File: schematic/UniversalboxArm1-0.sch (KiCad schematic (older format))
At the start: 170 parts, among them J1 USB_B_Micro, J110 Conn_01x03_Male, J120 Conn_02x04_Counter_Clockwise, J121 Conn_01x02_Male, J20 AVR-ISP-6, J50 Conn_01x14_Female, J60 Conn_01x06_Female, J61 Conn_02x08_Odd_Even, J62 Conn_02x04_Odd_Even, J90 Conn_02x03_Odd_Even, J91 Conn_02x04_Odd_Even, K90 IM01, K91 IM01, K92 IM01, K93 IM01, Q120 IRLML6402, Q20 BCX56-16, Q21 BSS138, Q22 BSS138, Q23 IRLML6402, Q24 IRLML6402, Q25 BSS138, Q50 IRLML6402, Q51 IRLML6402, Q60 BSS138, Q61 BSS138, Q62 BSS138, Q90 BSS138, Q91 BSS138, Q92 BSS138, Q93 BSS138, SW60 SW_SPST, SW61 SW_SPST, SW62 SW_SPST, SW63 SW_SPST, U1 USBLC6-2SC6, U110 MAX3221, U130 TSOP312xx, U2 LP38693MP-3.3, U20 ATtiny861A-SU, U21 REF3020, U22 MCP6542, U50 AT45DB641-S, U60 STM32L452RETx, U61 MCP65R41T-1202E, Y60 16MHz, Y61 32768Hz

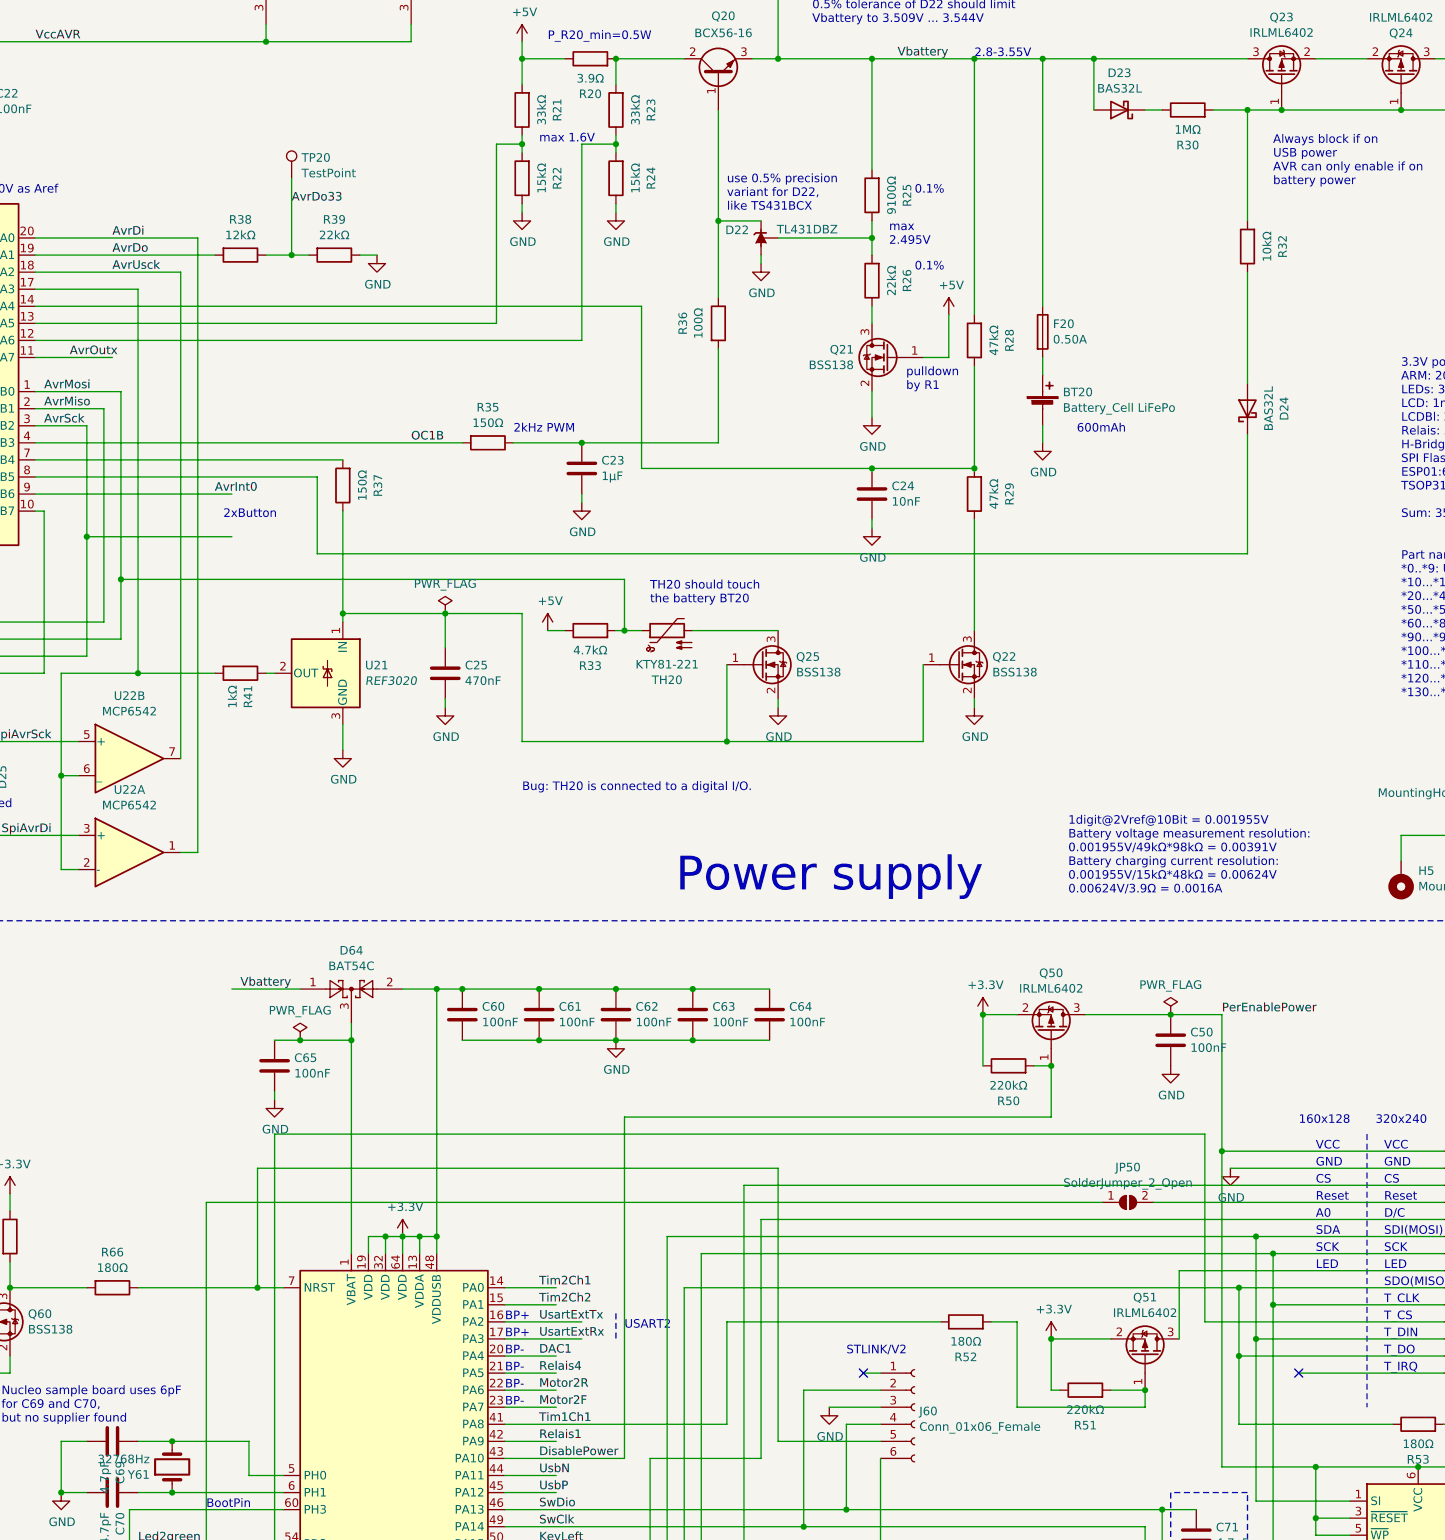
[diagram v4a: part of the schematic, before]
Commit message: Update schematic to version 1 revision 0.5 Reflecting issues found while getting pcb to work
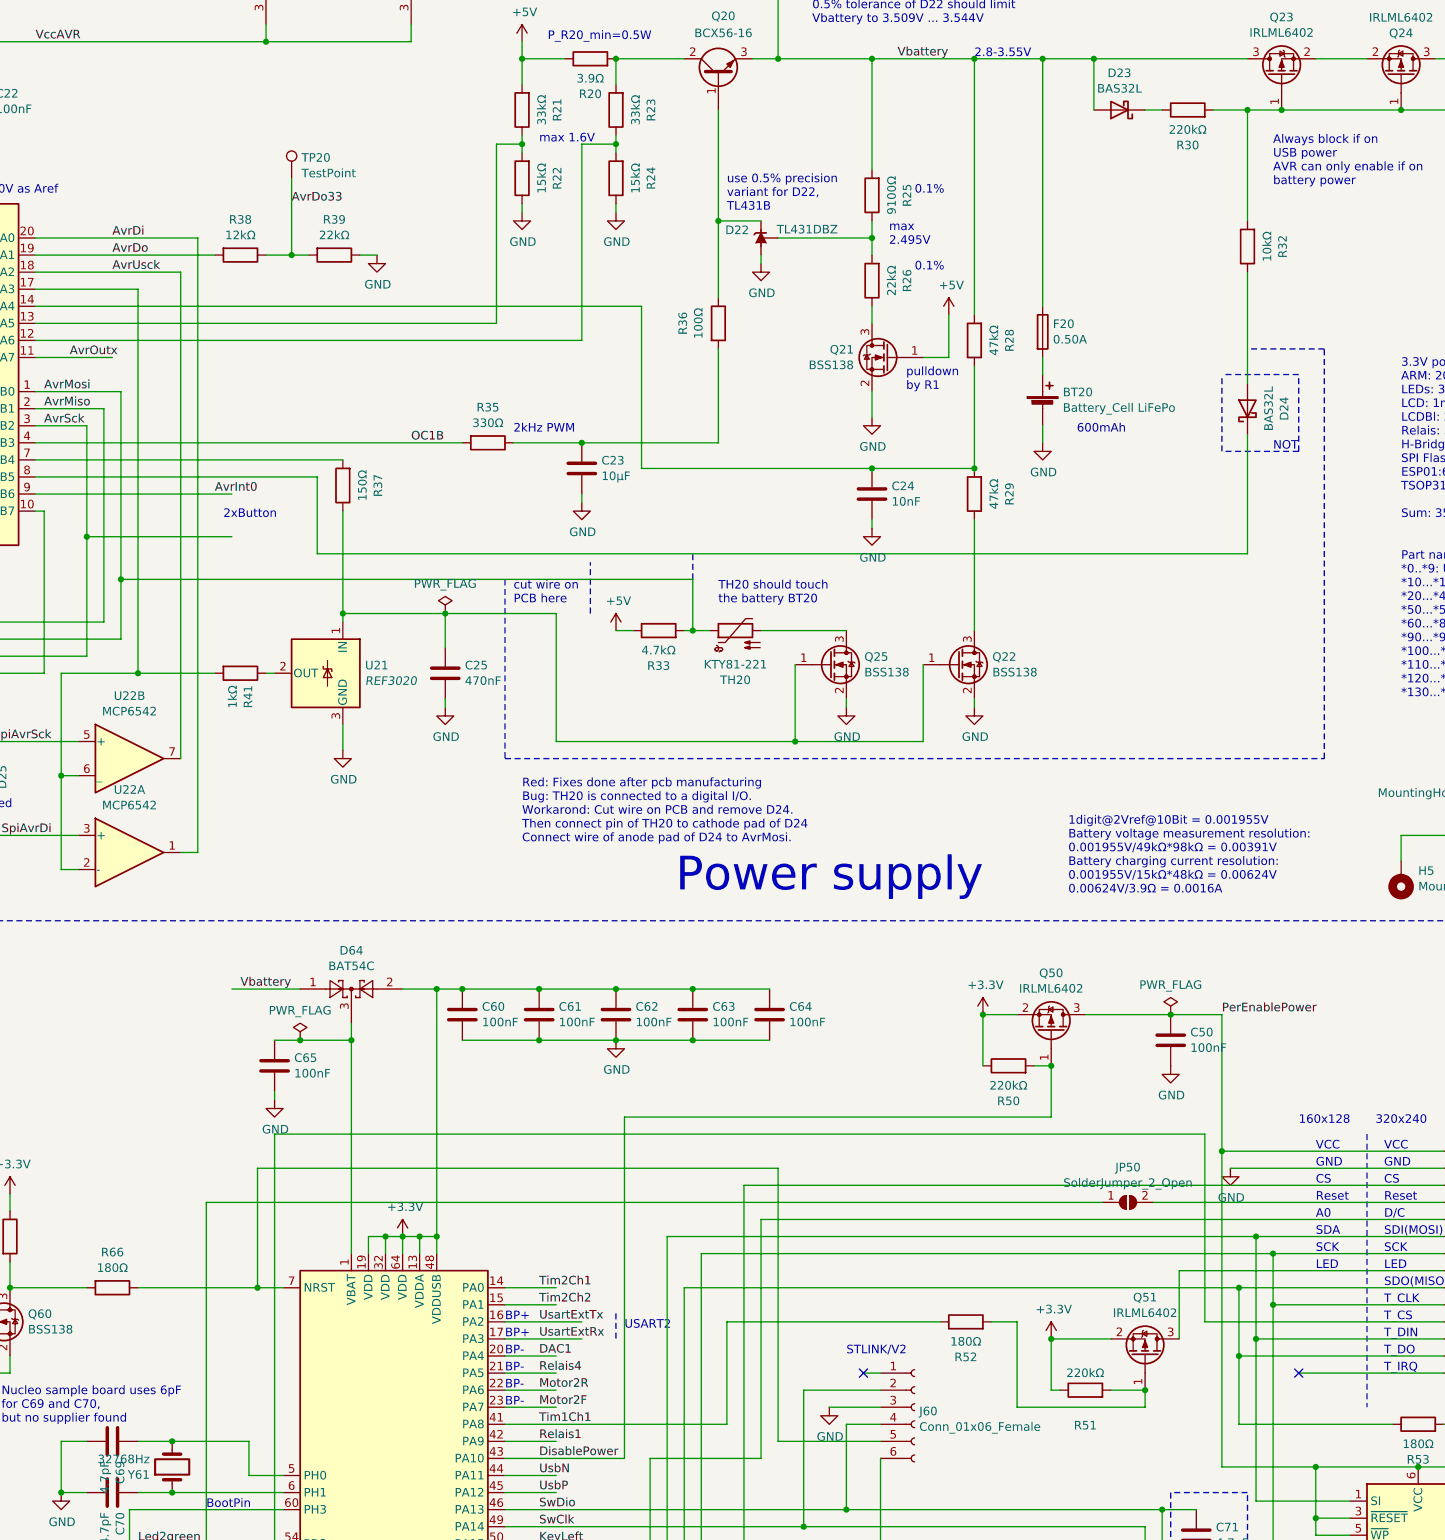
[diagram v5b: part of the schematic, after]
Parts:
- C23: value 1µF -> 10µF
- R30: value 1MΩ -> 220kΩ
- R35: value 150Ω -> 330Ω
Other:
- note added: "NOT"
- note added: "Red: Fixes done after pcb manufacturing\nBug: TH20 is connected to a digital I/O.\nWorkarond: Cut wire on PCB and remove D24.\nThen connect pin of TH20 to cathode pad of D24\nConnect wire of anode pad of D24 to AvrMosi."
- note added: "cut wire on\nPCB here"
- note added: "use 0.5% precision\nvariant for D22,\nTL431B\n"
- note removed: "Bug: TH20 is connected to a digital I/O."
- note removed: "use 0.5% precision\nvariant for D22,\nlike TS431BCX\n"
- moved on the sheet: Q25, R33, TH20
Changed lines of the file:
@@
 Sheet 1 1
 Title ""
-Date "2021-12-04"
-Rev "0.4"
+Date "2021-12-18"
+Rev "0.5"
 Comp ""
 Comment1 ""
@@
 P 4950 5450
 F 0 "R35" V 4743 5450 50  0000 C CNN
-F 1 "150Ω" V 4834 5450 50  0000 C CNN
+F 1 "330Ω" V 4834 5450 50  0000 C CNN
 F 2 "Resistor_SMD:R_0805_2012Metric_Pad1.15x1.40mm_HandSolder" V 4880 5450 50  0001 C CNN
 F 3 "~" H 4950 5450 50  0001 C CNN
@@
 P 5500 5600
 F 0 "C23" H 5615 5646 50  0000 L CNN
-F 1 "1µF" H 5615 5555 50  0000 L CNN
+F 1 "10µF" H 5615 5555 50  0000 L CNN
 F 2 "Capacitor_SMD:C_0805_2012Metric_Pad1.15x1.40mm_HandSolder" H 5538 5450 50  0001 C CNN
 F 3 "~" H 5500 5600 50  0001 C CNN
@@
 P 9050 3500
 F 0 "R30" V 8843 3500 50  0000 C CNN
-F 1 "1MΩ" V 8934 3500 50  0000 C CNN
+F 1 "220kΩ" V 8934 3500 50  0000 C CNN
 F 2 "Resistor_SMD:R_0805_2012Metric_Pad1.15x1.40mm_HandSolder" V 8980 3500 50  0001 C CNN
 F 3 "~" H 9050 3500 50  0001 C CNN
@@
 	6300 4150 6550 4150
 Text Notes 6350 4100 0    50   ~ 0
-use 0.5% precision\nvariant for D22,\nlike TS431BCX\n
+use 0.5% precision\nvariant for D22,\nTL431B\n
 $Comp
 L power:GND #PWR0121
@@
 L power:GND #PWR0124
 U 1 1 60A081EA
-P 6650 7000
-F 0 "#PWR0124" H 6650 6750 50  0001 C CNN
-F 1 "GND" H 6655 6827 50  0000 C CNN
-F 2 "" H 6650 7000 50  0001 C CNN
-F 3 "" H 6650 7000 50  0001 C CNN
-	1    6650 7000
+P 7050 7000
+F 0 "#PWR0124" H 7050 6750 50  0001 C CNN
+F 1 "GND" H 7055 6827 50  0000 C CNN
+F 2 "" H 7050 7000 50  0001 C CNN
+F 3 "" H 7050 7000 50  0001 C CNN
+	1    7050 7000
 	1    0    0    -1
 $EndComp
@@
 	6650 4250 7200 4250
 Wire Wire Line
-	6650 7000 6650 6950
+	7050 7000 7050 6950
 $Comp
 L Device:C C24
@@
 L Device:R R33
 U 1 1 609D221A
-P 5550 6550
-F 0 "R33" V 5343 6550 50  0000 C CNN
-F 1 "4.7kΩ" V 5434 6550 50  0000 C CNN
-F 2 "Resistor_SMD:R_0805_2012Metric_Pad1.15x1.40mm_HandSolder" V 5480 6550 50  0001 C CNN
-F 3 "~" H 5550 6550 50  0001 C CNN
-	1    5550 6550
+P 5950 6550
+F 0 "R33" V 5743 6550 50  0000 C CNN
+F 1 "4.7kΩ" V 5834 6550 50  0000 C CNN
+F 2 "Resistor_SMD:R_0805_2012Metric_Pad1.15x1.40mm_HandSolder" V 5880 6550 50  0001 C CNN
+F 3 "~" H 5950 6550 50  0001 C CNN
+	1    5950 6550
 	0    -1   -1   0
 $EndComp
-Text Notes 5900 6400 0    50   ~ 0
+Text Notes 6300 6400 0    50   ~ 0
 TH20 should touch\nthe battery BT20
 Text Label 3350 5750 0    50   ~ 0
@@
 	9400 6100 9400 5400
 Wire Wire Line
-	5850 6550 5750 6550
+	6250 6550 6150 6550
 $Comp
 L power:+5V #PWR0140
 U 1 1 60B19109
-P 5300 6550
-F 0 "#PWR0140" H 5300 6400 50  0001 C CNN
-F 1 "+5V" H 5315 6723 50  0000 C CNN
-F 2 "" H 5300 6550 50  0001 C CNN
-F 3 "" H 5300 6550 50  0001 C CNN
-	1    5300 6550
+P 5700 6550
+F 0 "#PWR0140" H 5700 6400 50  0001 C CNN
+F 1 "+5V" H 5715 6723 50  0000 C CNN
+F 2 "" H 5700 6550 50  0001 C CNN
+F 3 "" H 5700 6550 50  0001 C CNN
+	1    5700 6550
 	1    0    0    -1
 $EndComp
 Wire Wire Line
-	5400 6550 5300 6550
-Connection ~ 5750 6550
+	5800 6550 5700 6550
+Connection ~ 6150 6550
 Wire Wire Line
-	5750 6550 5700 6550
+	6150 6550 6100 6550
 Wire Wire Line
-	5150 6450 5150 7200
+	5350 6450 5350 7200
 Wire Wire Line
-	5150 7200 6350 7200
+	5350 7200 6750 7200
 Wire Wire Line
-	4700 6450 5150 6450
+	4700 6450 5350 6450
 Connection ~ 4700 6450
 $Comp
 L Sensor_Temperature:KTY81 TH20
 U 1 1 60B8406D
-P 6000 6550
-F 0 "TH20" V 5710 6550 50  0000 C CNN
-F 1 "KTY81-221" V 5801 6550 50  0000 C CNN
-F 2 "Package_TO_SOT_THT:TO-92-2" V 6200 6550 50  0001 C CNN
-F 3 "http://www.nxp.com/documents/data_sheet/KTY81_SER.pdf" H 6000 6500 50  0001 C CNN
-	1    6000 6550
+P 6400 6550
+F 0 "TH20" V 6110 6550 50  0000 C CNN
+F 1 "KTY81-221" V 6201 6550 50  0000 C CNN
+F 2 "Package_TO_SOT_THT:TO-92-2" V 6600 6550 50  0001 C CNN
+F 3 "http://www.nxp.com/documents/data_sheet/KTY81_SER.pdf" H 6400 6500 50  0001 C CNN
+	1    6400 6550
 	0    -1   -1   0
 $EndComp
@@
 AvrDo33
 Wire Wire Line
-	2800 6250 5750 6250
+	2800 6250 6150 6250
 Connection ~ 2800 6250
 Wire Wire Line
 	2800 6250 2800 6600
 Wire Wire Line
-	5750 6250 5750 6550
+	6150 6250 6150 6550
 Wire Wire Line
 	2300 4950 2750 4950
@@
 L Transistor_FET:BSS138 Q25
 U 1 1 60B55064
-P 6550 6750
-F 0 "Q25" H 6755 6796 50  0000 L CNN
-F 1 "BSS138" H 6755 6705 50  0000 L CNN
-F 2 "Package_TO_SOT_SMD:SOT-23" H 6750 6675 50  0001 L CIN
-F 3 "https://www.fairchildsemi.com/datasheets/BS/BSS138.pdf" H 6550 6750 50  0001 L CNN
-	1    6550 6750
+P 6950 6750
+F 0 "Q25" H 7155 6796 50  0000 L CNN
+F 1 "BSS138" H 7155 6705 50  0000 L CNN
+F 2 "Package_TO_SOT_SMD:SOT-23" H 7150 6675 50  0001 L CIN
+F 3 "https://www.fairchildsemi.com/datasheets/BS/BSS138.pdf" H 6950 6750 50  0001 L CNN
+	1    6950 6750
 	1    0    0    -1
 $EndComp
@@
 $EndComp
 Wire Wire Line
-	6150 6550 6650 6550
+	6550 6550 7050 6550
 Wire Wire Line
-	6350 6750 6350 7200
-Connection ~ 6350 7200
+	6750 6750 6750 7200
+Connection ~ 6750 7200
 $Comp
 L power:GND #PWR0144
@@
 P 8450 11000
 F 0 "R51" V 8243 11000 50  0000 C CNN
-F 1 "220kΩ" V 8334 11000 50  0000 C CNN
+F 1 "220kΩ" V 8550 11000 50  0000 C CNN
 F 2 "Resistor_SMD:R_0805_2012Metric_Pad1.15x1.40mm_HandSolder" V 8380 11000 50  0001 C CNN
 F 3 "~" H 8450 11000 50  0001 C CNN
@@
 Text Notes 10300 6950 0    50   ~ 0
 Part naming conventions:\n*0..*9: USB Vin\n*10...*19: reserved\n*20...*49: Battery Vin\n*50...*59: LCD and flash\n*60...*89: ARM CPU + basics\n*90...*99: Relais\n*100...*109: Reserved\n*110...*119: RS232\n*120...*129: ESP-01\n*130...*139: TSOP31236
-Text Notes 5150 7500 0    50   ~ 0
-Bug: TH20 is connected to a digital I/O.
+Text Notes 5150 7800 0    50   ~ 0
+Red: Fixes done after pcb manufacturing\nBug: TH20 is connected to a digital I/O.\nWorkarond: Cut wire on PCB and remove D24.\nThen connect pin of TH20 to cathode pad of D24\nConnect wire of anode pad of D24 to AvrMosi.
 Wire Wire Line
 	9300 1400 9900 1400
@@
 	7500 6750 7500 7200
 Wire Wire Line
-	6350 7200 7500 7200
+	6750 7200 7500 7200
 Wire Wire Line
 	6650 3200 6650 2800
@@
 Wire Wire Line
 	3100 1350 3100 1850
-Wire Notes Line rgb(255, 0, 0)
+Wire Notes Line width 12 rgb(255, 0, 0)
 	11100 3000 11550 3000
-Wire Notes Line rgb(255, 0, 0)
+Wire Notes Line width 12 rgb(255, 0, 0)
 	11550 3000 11550 3450
-Wire Notes Line rgb(255, 0, 0)
+Wire Notes Line width 12 rgb(255, 0, 0)
 	11550 3450 11100 3450
-Wire Notes Line rgb(255, 0, 0)
+Wire Notes Line width 12 rgb(255, 0, 0)
 	11100 3450 11100 3000
 Text Notes 11100 3700 0    50   ~ 0
@@
 	11700 3500 11700 3400
 Connection ~ 11200 3500
+Wire Notes Line width 12 rgb(255, 0, 0)
+	9700 5500 9250 5500
+Wire Notes Line width 12 rgb(255, 0, 0)
+	9250 5500 9250 5050
+Wire Notes Line width 12 rgb(255, 0, 0)
+	5550 6450 5550 6150
+Text Notes 5100 6400 0    50   ~ 0
+cut wire on\nPCB here
+Wire Notes Line width 12 rgb(255, 0, 0)
+	9700 5050 9250 5050
+Wire Notes Line width 12 rgb(255, 0, 0)
+	9700 5500 9700 5050
+Wire Notes Line width 12 style solid rgb(255, 0, 0)
+	6150 6250 6150 6100
+Text Notes 9550 5500 0    50   ~ 0
+NOT
+Wire Notes Line style solid rgb(255, 0, 0)
+	5050 6250 5050 7300
+Wire Notes Line style solid rgb(255, 0, 0)
+	5050 7300 9850 7300
+Wire Notes Line style solid rgb(255, 0, 0)
+	9850 7300 9850 4900
+Wire Notes Line style solid rgb(255, 0, 0)
+	9850 4900 9400 4900
 $EndSCHEMATC

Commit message: Schematic: Rearrange text to avoid overlapping with wires
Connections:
- wire segments 756 -> 758
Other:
- note added: "1,9kHz PWM"
- note added: "Checked for the STM32L45xxx:\nBP+: Bootloader drives this pin as pull-up\nBP-: Bootloader drives this pin as pull-down\nRP+: Bootloader and reset drives this pin as pull-up"
- note added: "RP+"
- note added: "STM Usart3Rx\nclose 3-2 of JP60 for STM32L\nclose 1-2 for STM F4, F7, H7 and\nset RX<->TX switch bit there"
- note removed: "2kHz PWM"
- note removed: "Checked for the STM32L45xxx:\nBP+: Bootloader drives this pin as pull-up\nBP-: Bootloader drives this pin as pull-down"
- note removed: "STM Usart3Rx\nclose 3-2 for STM32L\nclose 1-2 for STM F4, F7, H7 and\nset RX<->TX switch bit there"
- moved on the sheet: C71

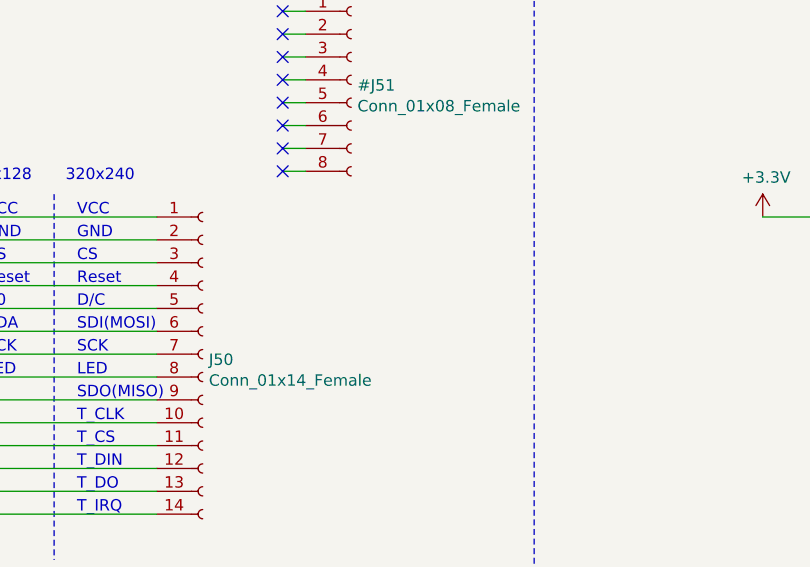
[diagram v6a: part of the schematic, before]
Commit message: STM32: Add testcode for using the LCD Schematic: Document the missing pullup on the reset line of the LCD BOM: Add missing capacitor
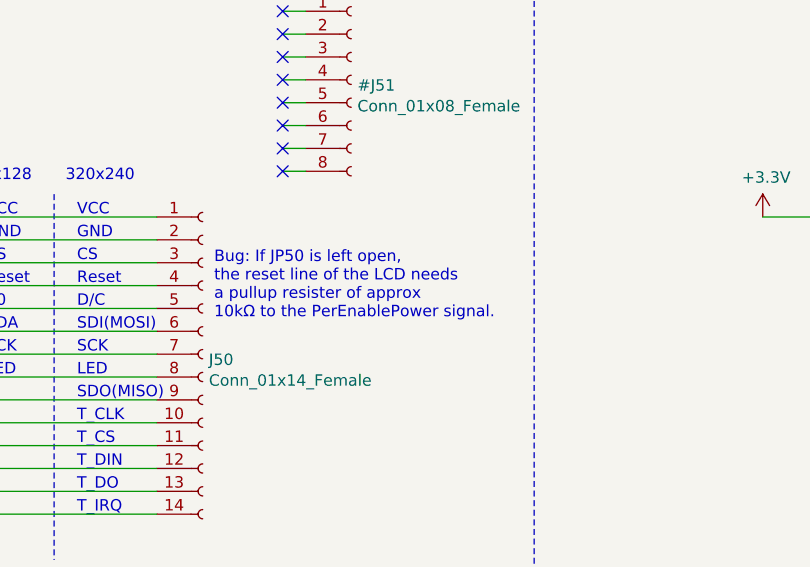
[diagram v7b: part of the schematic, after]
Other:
- note added: "Bug: If JP50 is left open,\nthe reset line of the LCD needs\na pullup resister of approx\n10kΩ to the PerEnablePower signal."
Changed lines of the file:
@@
 Sheet 1 1
 Title ""
-Date "2021-12-18"
-Rev "0.6"
+Date "2022-01-02"
+Rev "0.7"
 Comp ""
 Comment1 ""
@@
 Text Notes 5050 11700 0    50   ~ 0
 RP+
+Text Notes 10800 10050 0    50   ~ 0
+Bug: If JP50 is left open,\nthe reset line of the LCD needs\na pullup resister of approx\n10kΩ to the PerEnablePower signal.
 $EndSCHEMATC
